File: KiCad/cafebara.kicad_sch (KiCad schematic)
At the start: 54 parts, among them J1 Micro_SD_Card_Det2, J2 USB_C_Receptacle_USB2.0_14P, J3 PROG, J4 Conn_01x19_MountingPin, J5 I2C, J6 EDID, Q1 NMOS, SW1 SW_Push, U3 ATtiny1616-M, U4 M24C02-WMN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

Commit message: Various improvements and misc changes
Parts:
- removed U4: M24C02-WMN, Package_SO:SOIC-8_3.9x4.9mm_P1.27mm, symbol Memory_EEPROM:M24C02-WMN
- added C17, C18: 22uF, Capacitor_SMD:C_0402_1005Metric, symbol Device:C_Small
- added R9: 1k, Resistor_SMD:R_0402_1005Metric, symbol Device:R_Small
- added U4: M24C02-RMC, cafebara:UFDFPN_RMC, symbol Memory_EEPROM:M24C02-FDW
- C10, C11: value 10uF -> 22uF; footprint Capacitor_SMD:C_0402_1005Metric -> Capacitor_SMD:C_0805_2012Metric
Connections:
- net +5V: now also R9.2, U4.8 (VCC)
- net EEPROM_~{WC}: now also R9.1, U4.7 (~{WC})
- net EN: now also U3.18 (PC3); no longer U3.9 (PB5)
- net GND: now also C17.2, C18.2, U4.1 (E0), U4.2 (E1), U4.3 (E2), U4.4 (VSS), U4.9 (VSS)
- net HDMI_SCL: now also U4.6 (SCL)
- net HDMI_SDA: now also U4.5 (SDA)
- net LED: now also U3.20 (PA1); no longer U3.6 (PA5)
- net VCC: now also C17.1, C18.1
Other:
- moved on the sheet: R4, TP3

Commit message: Misc improvements, 3D model generation
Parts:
- removed C10: 22uF, Capacitor_SMD:C_0805_2012Metric, symbol Device:C_Small
- added C19: 100uF, Capacitor_Tantalum_SMD:CP_EIA-3216-10_Kemet-I, symbol Device:C_Polarized_Small
- C6: footprint Capacitor_SMD:C_0603_1608Metric -> Capacitor_SMD:C_0402_1005Metric
- J1: symbol Connector:Micro_SD_Card_Det2 -> Connector:Micro_SD_Card_Det1
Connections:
- net GND: now also J1.10 (SHIELD), C19.2; no longer J1.9 (DET_B)
- net SD_DECT: now also J1.9 (DET); no longer J1.10 (DET_A)
- net VCC: now also C19.1
- net ~{ALERT}: now also U3.9 (PB5); no longer U3.11 (PB3)
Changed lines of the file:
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@@
 	)
 	(junction
-		(at -96.52 96.52)
-		(diameter 0)
-		(color 0 0 0 0)
-	)
-	(junction
 		(at 224.79 66.04)
 		(diameter 0)
@@
 	)
 	(junction
+		(at -96.52 96.52)
+		(diameter 0)
+		(color 0 0 0 0)
+	)
+	(junction
 		(at 113.03 34.29)
 		(diameter 0)
@@
 		(color 0 0 0 0)
 	)
-	(junction
-		(at 224.79 156.21)
-		(diameter 0)
-		(color 0 0 0 0)
-	)
 	(no_connect
 		(at -137.16 96.52)
 	)
 	(no_connect
-		(at 217.17 78.74)
-	)
-	(no_connect
 		(at -137.16 127)
 	)
@@
 	)
 	(no_connect
+		(at 217.17 73.66)
+	)
+	(no_connect
 		(at -137.16 121.92)
 	)
@@
 	(wire
 		(pts
-			(xy 224.79 156.21) (xy 237.49 156.21)
-		)
-		(stroke
-			(width 0)
-			(type default)
-		)
-	)
-	(wire
-		(pts
 			(xy 50.8 116.84) (xy 54.61 116.84)
 		)
@@
 	(wire
 		(pts
-			(xy 219.71 73.66) (xy 217.17 73.66)
+			(xy 219.71 78.74) (xy 217.17 78.74)
 		)
 		(stroke
@@
 	(wire
 		(pts
-			(xy 224.79 156.21) (xy 224.79 160.02)
+			(xy 224.79 146.05) (xy 224.79 160.02)
 		)
 		(stroke
@@
 	(wire
 		(pts
-			(xy 80.01 171.45) (xy 77.47 171.45)
+			(xy -96.52 96.52) (xy -87.63 96.52)
 		)
 		(stroke
@@
 	(wire
 		(pts
-			(xy 217.17 45.72) (xy 228.6 45.72)
+			(xy 80.01 171.45) (xy 77.47 171.45)
 		)
 		(stroke
@@
 	(wire
 		(pts
-			(xy 219.71 71.12) (xy 217.17 71.12)
+			(xy 217.17 45.72) (xy 228.6 45.72)
 		)
 		(stroke
@@
 	(wire
 		(pts
-			(xy 191.77 128.27) (xy 191.77 130.81)
+			(xy 219.71 71.12) (xy 217.17 71.12)
 		)
 		(stroke
@@
 	(wire
 		(pts
-			(xy 116.84 158.75) (xy 113.03 158.75)
+			(xy 191.77 128.27) (xy 191.77 130.81)
 		)
 		(stroke
@@
 	(wire
 		(pts
-			(xy -96.52 96.52) (xy -87.63 96.52)
+			(xy 116.84 158.75) (xy 113.03 158.75)
 		)
 		(stroke
@@
 	(wire
 		(pts
-			(xy 224.79 146.05) (xy 224.79 156.21)
-		)
-		(stroke
-			(width 0)
-			(type default)
-		)
-	)
-	(wire
-		(pts
 			(xy -106.68 120.65) (xy -115.57 120.65)
 		)
@@
 	(global_label "SD_DECT"
 		(shape output)
-		(at 237.49 153.67 180)
+		(at 237.49 156.21 180)
 		(fields_autoplaced yes)
 		(effects
@@
 		)
 		(property "Intersheetrefs" "${INTERSHEET_REFS}"
-			(at 226.4011 153.67 0)
+			(at 226.4011 156.21 0)
 			(effects
 				(font
@@
 	(global_label "~{ALERT}"
 		(shape input)
-		(at 219.71 73.66 0)
+		(at 219.71 78.74 0)
 		(fields_autoplaced yes)
 		(effects
@@
 		)
 		(property "Intersheetrefs" "${INTERSHEET_REFS}"
-			(at 228.1985 73.66 0)
+			(at 228.1985 78.74 0)
 			(effects
 				(font
@@
 	)
 	(symbol
+		(lib_id "Device:C_Polarized_Small")
+		(at -96.52 99.06 0)
+		(mirror y)
+		(unit 1)
+		(exclude_from_sim no)
+		(in_bom yes)
+		(on_board yes)
+		(dnp no)
+		(property "Reference" "C19"
+			(at -100.33 97.2438 0)
+			(effects
+				(font
+					(size 1.27 1.27)
+				)
+				(justify left)
+			)
+		)
+		(property "Value" "100uF"
+			(at -100.33 99.7838 0)
+			(effects
+				(font
+					(size 1.27 1.27)
+				)
+				(justify left)
+			)
+		)
+		(property "Footprint" "Capacitor_Tantalum_SMD:CP_EIA-3216-10_Kemet-I"
+			(at -96.52 99.06 0)
+			(effects
+				(font
+					(size 1.27 1.27)
+				)
+				(hide yes)
+			)
+		)
+		(property "Datasheet" "~"
+			(at -96.52 99.06 0)
+			(effects
+				(font
+					(size 1.27 1.27)
+				)
+				(hide yes)
+			)
+		)
+		(property "Description" "Polarized capacitor, small symbol"
+			(at -96.52 99.06 0)
+			(effects
+				(font
+					(size 1.27 1.27)
+				)
+				(hide yes)
+			)
+		)
+		(property "Digikey" "https://www.digikey.com.au/en/products/detail/vishay-sprague/TL8A0107M6R3C/3883158"
+			(at -96.52 99.06 0)
+			(effects
+				(font
+					(size 1.27 1.27)
+				)
+				(hide yes)
+			)
+		)
+		(pin "2"
+		)
+		(pin "1"
+		)
+		(instances
+			(project ""
+				(path "/dcc89f95-4ae4-4756-aa81-33bf4d3c86ca"
+					(reference "C19")
+					(unit 1)
+				)
+			)
+		)
+	)
+	(symbol
 		(lib_id "power:GND")
 		(at 45.72 160.02 0)
@@
 			)
 		)
-		(property "Footprint" "Capacitor_SMD:C_0603_1608Metric"
+		(property "Footprint" "Capacitor_SMD:C_0402_1005Metric"
 			(at 148.59 158.75 0)
 			(effects
@@
 	)
 	(symbol
-		(lib_id "Device:C_Small")
-		(at -96.52 99.06 0)
-		(mirror y)
-		(unit 1)
-		(exclude_from_sim no)
-		(in_bom yes)
-		(on_board yes)
-		(dnp no)
-		(property "Reference" "C10"
-			(at -99.06 97.7962 0)
-			(effects
-				(font
-					(size 1.27 1.27)
-				)
-				(justify left)
-			)
-		)
-		(property "Value" "22uF"
-			(at -99.06 100.3362 0)
-			(effects
-				(font
-					(size 1.27 1.27)
-				)
-				(justify left)
-			)
-		)
-		(property "Footprint" "Capacitor_SMD:C_0805_2012Metric"
-			(at -96.52 99.06 0)
-			(effects
-				(font
-					(size 1.27 1.27)
-				)
-				(hide yes)
-			)
-		)
-		(property "Datasheet" "~"
-			(at -96.52 99.06 0)
-			(effects
-				(font
-					(size 1.27 1.27)
-				)
-				(hide yes)
-			)
-		)
-		(property "Description" "Unpolarized capacitor, small symbol"
-			(at -96.52 99.06 0)
-			(effects
-				(font
-					(size 1.27 1.27)
-				)
-				(hide yes)
-			)
-		)
-		(pin "1"
-		)
-		(pin "2"
-		)
-		(instances
-			(project "cafebara"
-				(path "/dcc89f95-4ae4-4756-aa81-33bf4d3c86ca"
-					(reference "C10")
-					(unit 1)
-				)
-			)
-		)
-	)
-	(symbol
 		(lib_id "power:GND")
 		(at 224.79 160.02 0)
@@
 	)
 	(symbol
-		(lib_id "Connector:Micro_SD_Card_Det2")
+		(lib_id "Connector:Micro_SD_Card_Det1")
 		(at 260.35 143.51 0)
 		(unit 1)
@@
 			)
 		)
-		(property "Description" "Micro SD Card Socket with two card detection pins"
+		(property "Description" "Micro SD Card Socket with one card detection pin"
 			(at 260.35 143.51 0)
 			(effects

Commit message: Several improvements
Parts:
- added C10: 10uF, Capacitor_SMD:C_0603_1608Metric, symbol Device:C_Small
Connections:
- net GND: now also C10.2
- net VBUS: now also C10.1
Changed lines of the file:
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@@
 	)
 	(junction
+		(at -168.91 99.06)
+		(diameter 0)
+		(color 0 0 0 0)
+	)
+	(junction
 		(at 62.23 156.21)
 		(diameter 0)
@@
 	)
 	(junction
+		(at -168.91 93.98)
+		(diameter 0)
+		(color 0 0 0 0)
+	)
+	(junction
 		(at 77.47 173.99)
 		(diameter 0)
@@
 	(wire
 		(pts
+			(xy -168.91 99.06) (xy -158.75 99.06)
+		)
+		(stroke
+			(width 0)
+			(type default)
+		)
+	)
+	(wire
+		(pts
 			(xy 116.84 171.45) (xy 113.03 171.45)
 		)
@@
 	(wire
 		(pts
+			(xy -168.91 93.98) (xy -158.75 93.98)
+		)
+		(stroke
+			(width 0)
+			(type default)
+		)
+	)
+	(wire
+		(pts
 			(xy 116.84 166.37) (xy 113.03 166.37)
 		)
@@
 					(unit 1)
 				)
+			)
+		)
+	)
+	(symbol
+		(lib_id "Device:C_Small")
+		(at -158.75 96.52 0)
+		(mirror y)
+		(unit 1)
+		(exclude_from_sim no)
+		(in_bom yes)
+		(on_board yes)
+		(dnp no)
+		(property "Reference" "C10"
+			(at -161.29 95.2562 0)
+			(effects
+				(font
+					(size 1.27 1.27)
+				)
+				(justify left)
+			)
+		)
+		(property "Value" "10uF"
+			(at -161.29 97.7962 0)
+			(effects
+				(font
+					(size 1.27 1.27)
+				)
+				(justify left)
+			)
+		)
+		(property "Footprint" "Capacitor_SMD:C_0603_1608Metric"
+			(at -158.75 96.52 0)
+			(effects
+				(font
+					(size 1.27 1.27)
+				)
+				(hide yes)
+			)
+		)
+		(property "Datasheet" "~"
+			(at -158.75 96.52 0)
+			(effects
+				(font
+					(size 1.27 1.27)
+				)
+				(hide yes)
+			)
+		)
+		(property "Description" "Unpolarized capacitor, small symbol"
+			(at -158.75 96.52 0)
+			(effects
+				(font
+					(size 1.27 1.27)
+				)
+				(hide yes)
+			)
+		)
+		(pin "1"
+		)
+		(pin "2"
+		)
+		(instances
+			(project "cafebara"
+				(path "/dcc89f95-4ae4-4756-aa81-33bf4d3c86ca"
+					(reference "C10")
+					(unit 1)
+				)

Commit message: Misc improvements to several boards
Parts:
- added C20: 10uF, Capacitor_SMD:C_0603_1608Metric, symbol Device:C_Small
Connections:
- net BATT: now also C20.1
- net GND: now also C20.2
- net ~{INT} renamed ~{BQ_INT}
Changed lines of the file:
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@@
 	)
 	(junction
+		(at -90.17 109.22)
+		(diameter 0)
+		(color 0 0 0 0)
+	)
+	(junction
 		(at 194.31 128.27)
 		(diameter 0)
@@
 	)
 	(junction
+		(at -90.17 116.84)
+		(diameter 0)
+		(color 0 0 0 0)
+	)
+	(junction
 		(at 232.41 68.58)
 		(diameter 0)
@@
 	(wire
 		(pts
+			(xy -80.01 110.49) (xy -80.01 109.22)
+		)
+		(stroke
+			(width 0)
+			(type default)
+		)
+	)
+	(wire
+		(pts
 			(xy 128.27 53.34) (xy 147.32 53.34)
 		)
@@
 	(wire
 		(pts
+			(xy -80.01 116.84) (xy -90.17 116.84)
+		)
+		(stroke
+			(width 0)
+			(type default)
+		)
+	)
+	(wire
+		(pts
 			(xy 201.93 26.67) (xy 218.44 26.67)
 		)
@@
 	(wire
 		(pts
+			(xy -80.01 115.57) (xy -80.01 116.84)
+		)
+		(stroke
+			(width 0)
+			(type default)
+		)
+	)
+	(wire
+		(pts
 			(xy 190.5 120.65) (xy 193.04 120.65)
 		)
@@
 	(wire
 		(pts
+			(xy -80.01 109.22) (xy -90.17 109.22)
+		)
+		(stroke
+			(width 0)
+			(type default)
+		)
+	)
+	(wire
+		(pts
 			(xy 201.93 26.67) (xy 201.93 38.1)
 		)
@@
 		)
 	)
-	(global_label "~{INT}"
+	(global_label "~{BQ_INT}"
 		(shape input)
 		(at 186.69 66.04 180)
@@
 		)
 		(property "Intersheetrefs" "${INTERSHEET_REFS}"
-			(at 180.8019 66.04 0)
+			(at 177.2338 66.04 0)
 			(effects
 				(font
@@
 		)
 	)
-	(global_label "~{INT}"
+	(global_label "~{BQ_INT}"
 		(shape output)
 		(at -137.16 119.38 180)
@@
 		)
 		(property "Intersheetrefs" "${INTERSHEET_REFS}"
-			(at -143.0481 119.38 0)
+			(at -146.6162 119.38 0)
 			(effects
 				(font
@@
 					(unit 1)
 				)
+			)
+		)
+	)
+	(symbol
+		(lib_id "Device:C_Small")
+		(at -80.01 113.03 0)
+		(unit 1)
+		(exclude_from_sim no)
+		(in_bom yes)
+		(on_board yes)
+		(dnp no)
+		(property "Reference" "C20"
+			(at -77.47 111.7662 0)
+			(effects
+				(font
+					(size 1.27 1.27)
+				)
+				(justify left)
+			)
+		)
+		(property "Value" "10uF"
+			(at -77.47 114.3062 0)
+			(effects
+				(font
+					(size 1.27 1.27)
+				)
+				(justify left)
+			)
+		)
+		(property "Footprint" "Capacitor_SMD:C_0603_1608Metric"
+			(at -80.01 113.03 0)
+			(effects
+				(font
+					(size 1.27 1.27)
+				)
+				(hide yes)
+			)
+		)
+		(property "Datasheet" "~"
+			(at -80.01 113.03 0)
+			(effects
+				(font
+					(size 1.27 1.27)
+				)
+				(hide yes)
+			)
+		)
+		(property "Description" "Unpolarized capacitor, small symbol"
+			(at -80.01 113.03 0)
+			(effects
+				(font
+					(size 1.27 1.27)
+				)
+				(hide yes)
+			)
+		)
+		(pin "1"
+		)
+		(pin "2"
+		)
+		(instances
+			(project "cafebara"
+				(path "/dcc89f95-4ae4-4756-aa81-33bf4d3c86ca"
+					(reference "C20")
+					(unit 1)
+				)

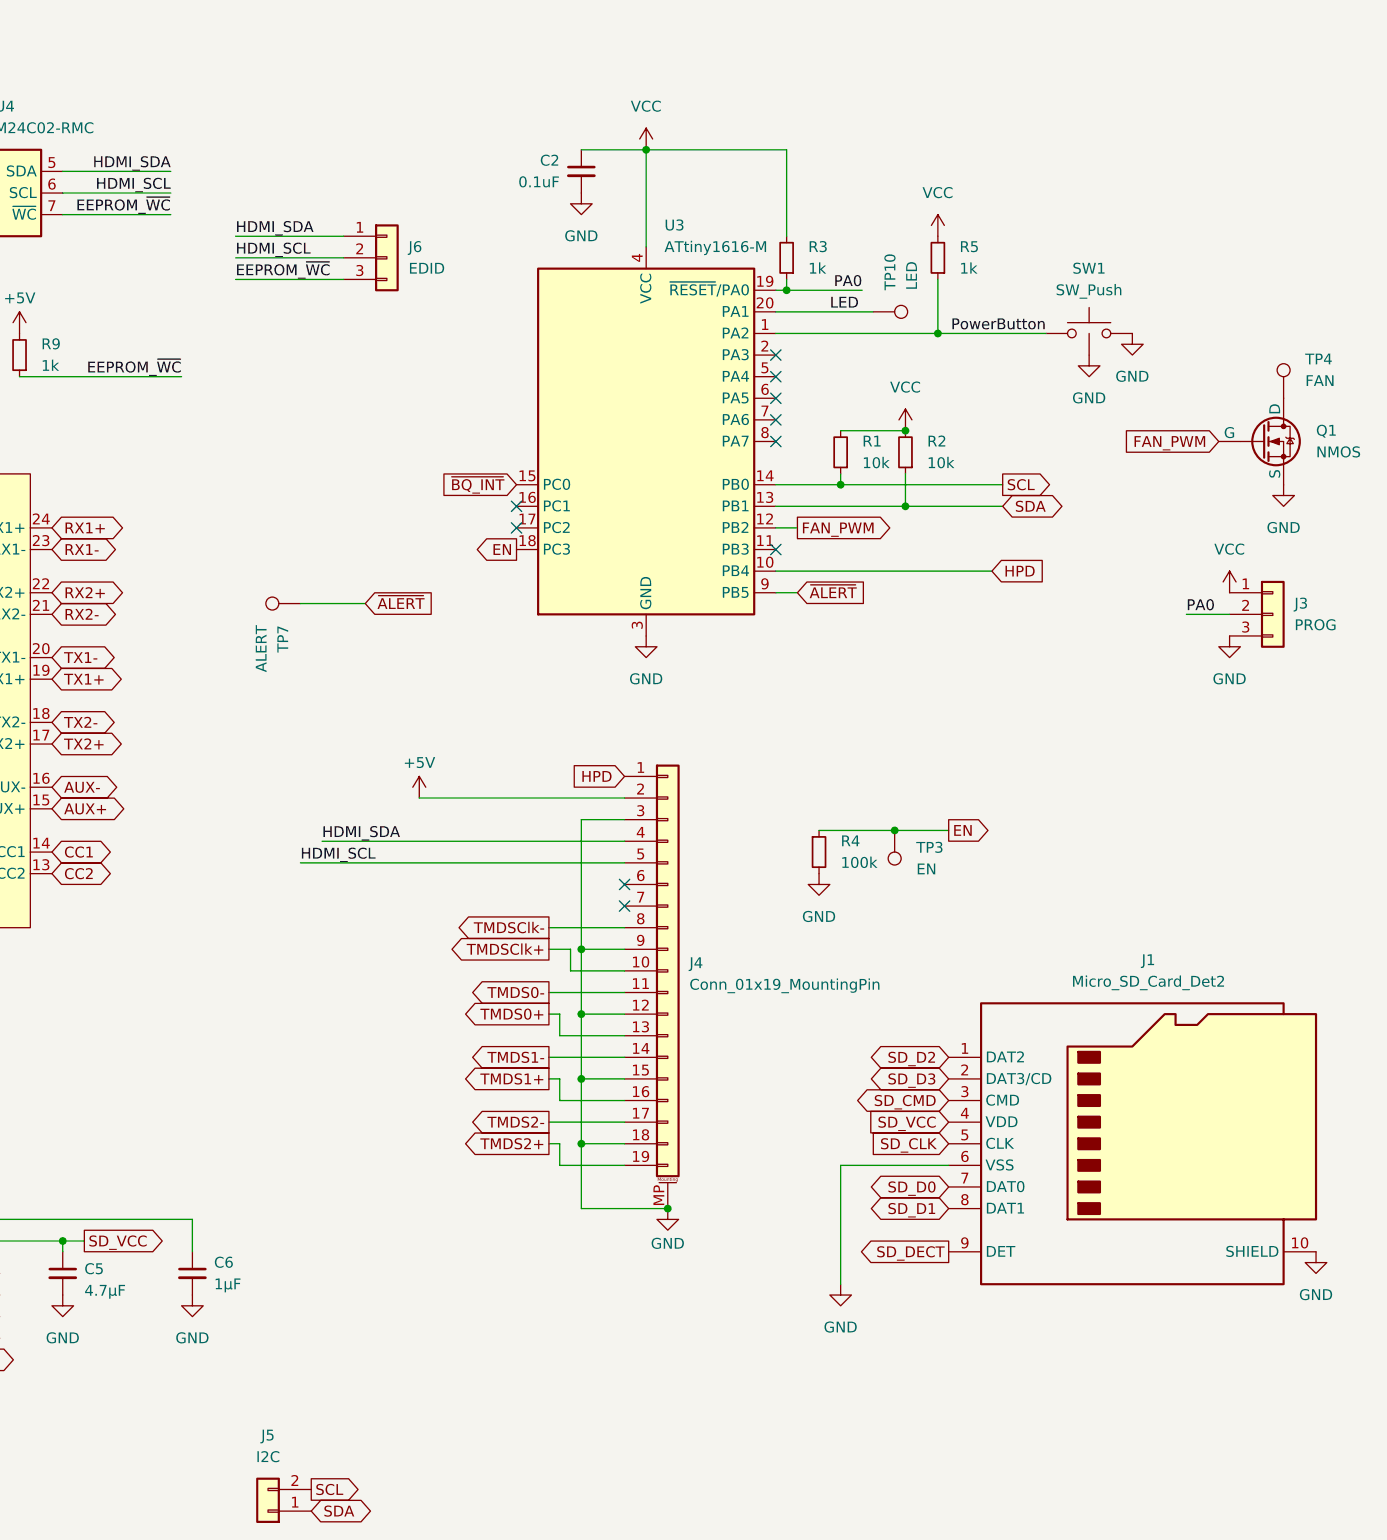
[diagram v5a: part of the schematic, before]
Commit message: Rework, adding UART for Pi communication
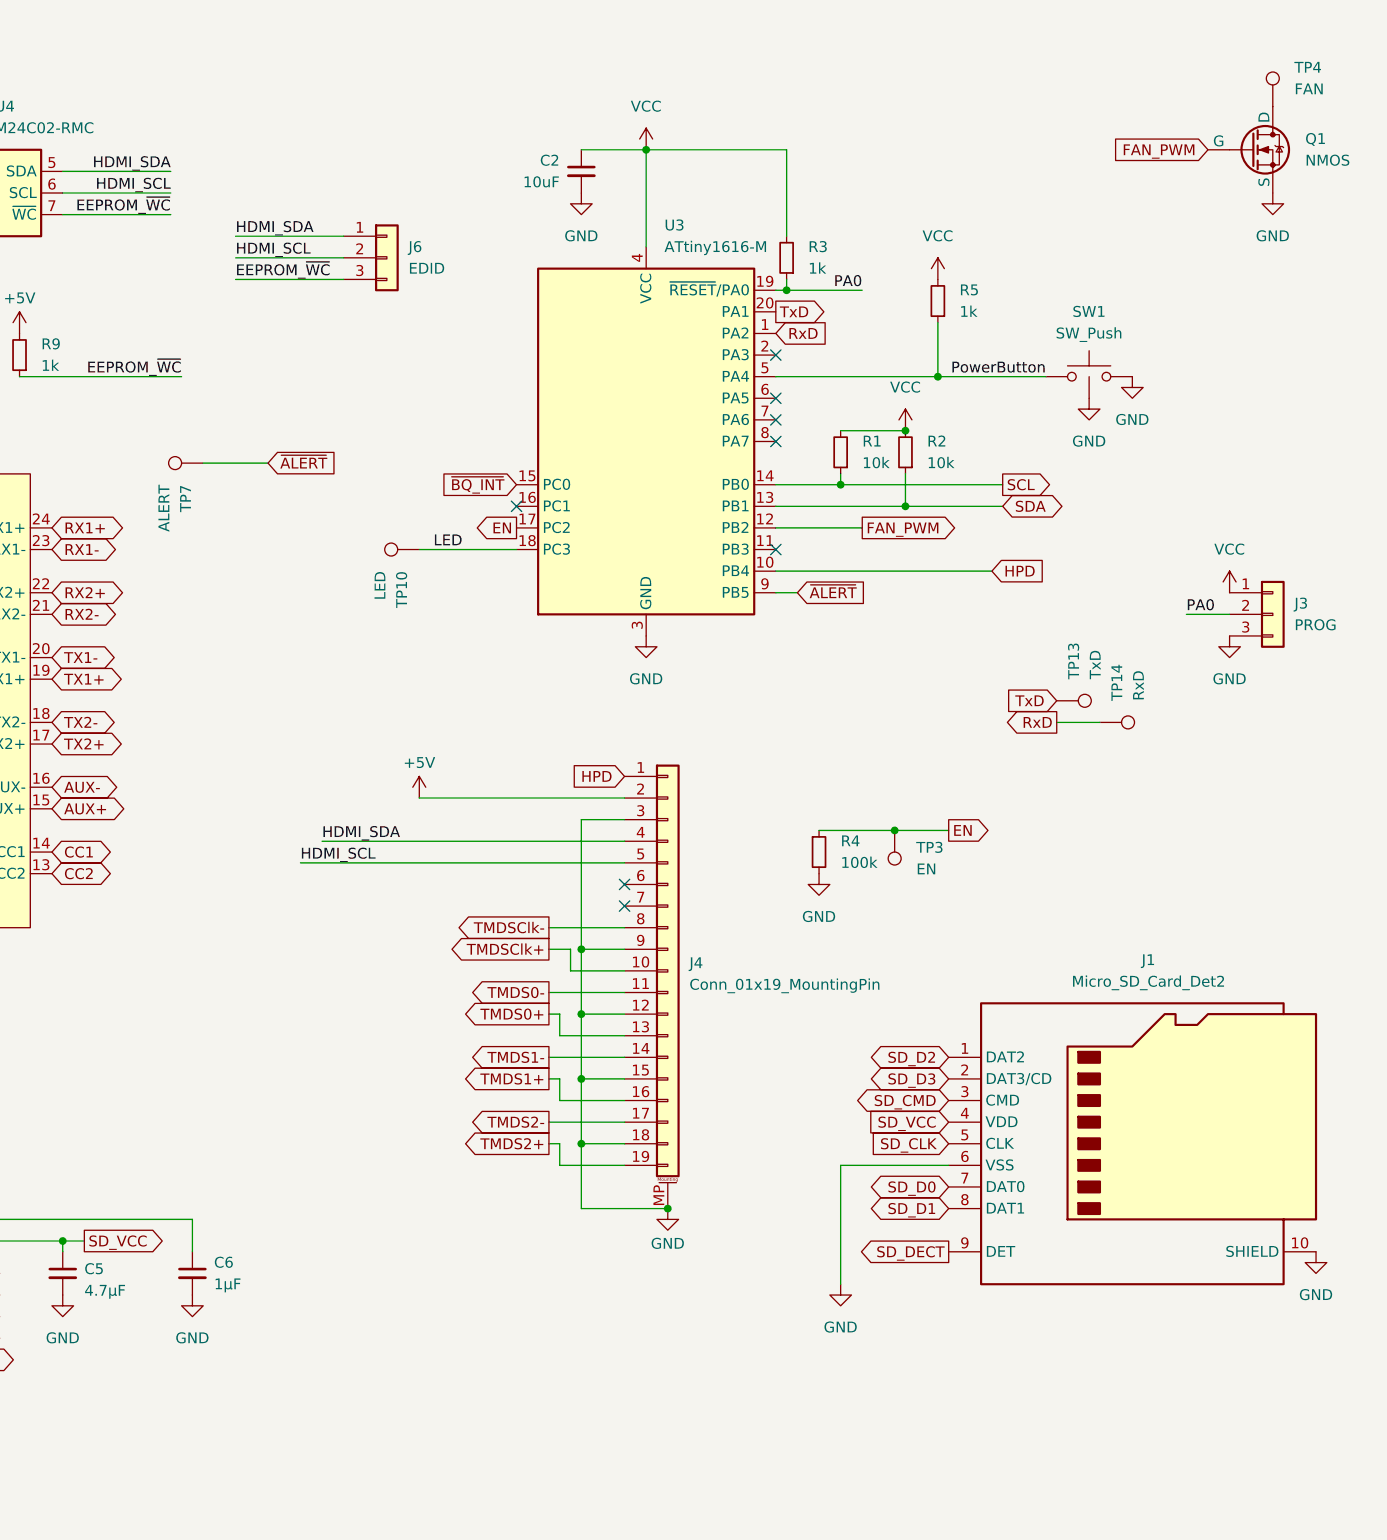
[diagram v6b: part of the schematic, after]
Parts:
- removed J5: I2C, Connector_PinSocket_1.00mm:PinSocket_1x02_P1.00mm_Vertical, symbol Connector_Generic:Conn_01x02
- added TP13: TxD, cafebara:TestPoint_Pad_D1.0mm_Small, symbol Connector:TestPoint
- added TP14: RxD, cafebara:TestPoint_Pad_D1.0mm_Small, symbol Connector:TestPoint
- C2: value 0.1uF -> 10uF; footprint Capacitor_SMD:C_0603_1608Metric -> Capacitor_SMD:C_0402_1005Metric
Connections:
- net EN: now also U3.17 (PC2); no longer U3.18 (PC3)
- net LED: now also U3.18 (PC3); no longer U3.20 (PA1)
- net PowerButton: now also U3.5 (PA4); no longer U3.1 (PA2)
- new net RxD: TP14.1, U3.1 (PA2)
- new net TxD: TP13.1, U3.20 (PA1)
- no-connect marks 19 -> 17
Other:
- moved on the sheet: Q1, R5, SW1, TP10, TP4, TP7
